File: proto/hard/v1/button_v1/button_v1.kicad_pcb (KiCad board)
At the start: 2 copper layers, 108.9 x 76.9 mm, 135 parts, among them J1 Conn_01x06_Female, J10 Conn_01x04_Male, J14 K3-2235D, J2 Conn_01x06_Female, J3 Conn_01x06_Female, J4 Conn_01x06_Female, J5 USB_B_Micro, J6 Conn_01x08_Female, J7 Conn_01x04_Female, J8 AudioJack3, J9 Conn_01x06_Male, Q1 TP0610T, Q2 IRLML2060, Q3 TP0610T, Q4 IRLML2060, Q5 IRLML2060, Q6 UMG8N, Q7 UMG8N, Q8 IRLML2803, Q9 TP0610T, U1 LCD_2.8_SPI, U10 NL27WZ14, U11 TC305, U12 LCD_1_8_SPI, U13 74HC595, U2 STM32F103C8Tx, U3 RT8009-33, U4 RClamp0554S, U5 RT9293, U6 LM339, U7 AP1117-33, U8 485, U9 LM358, Y1 8MHz

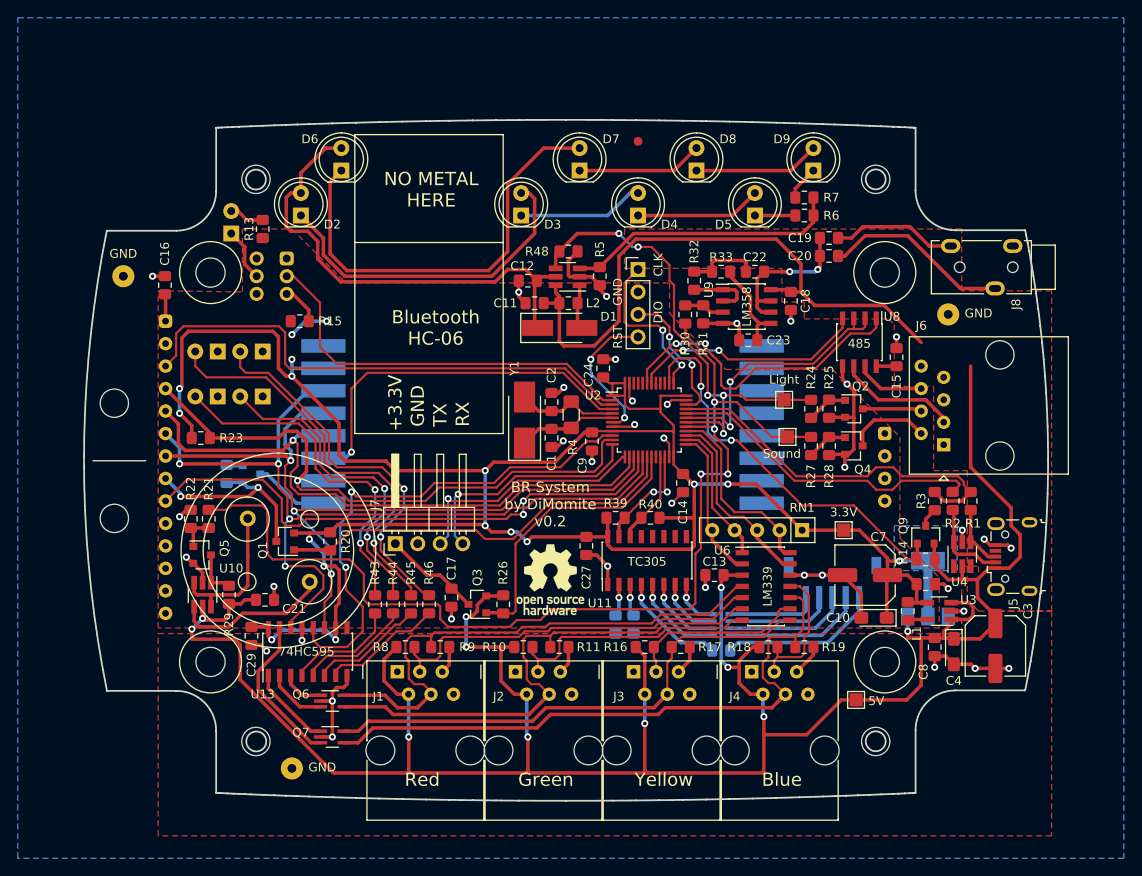
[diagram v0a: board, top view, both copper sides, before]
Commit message: Updated main board to v0.3: - changed power coils to bobbin - added test point for StartLED line - integrated new LCD screen footprint with LED power connectors - changed Schottky diode footprint to smaller in start LED converter - changed crystal footprint to smaller - added guard ring around crystal - disconnected USB shield from GND line
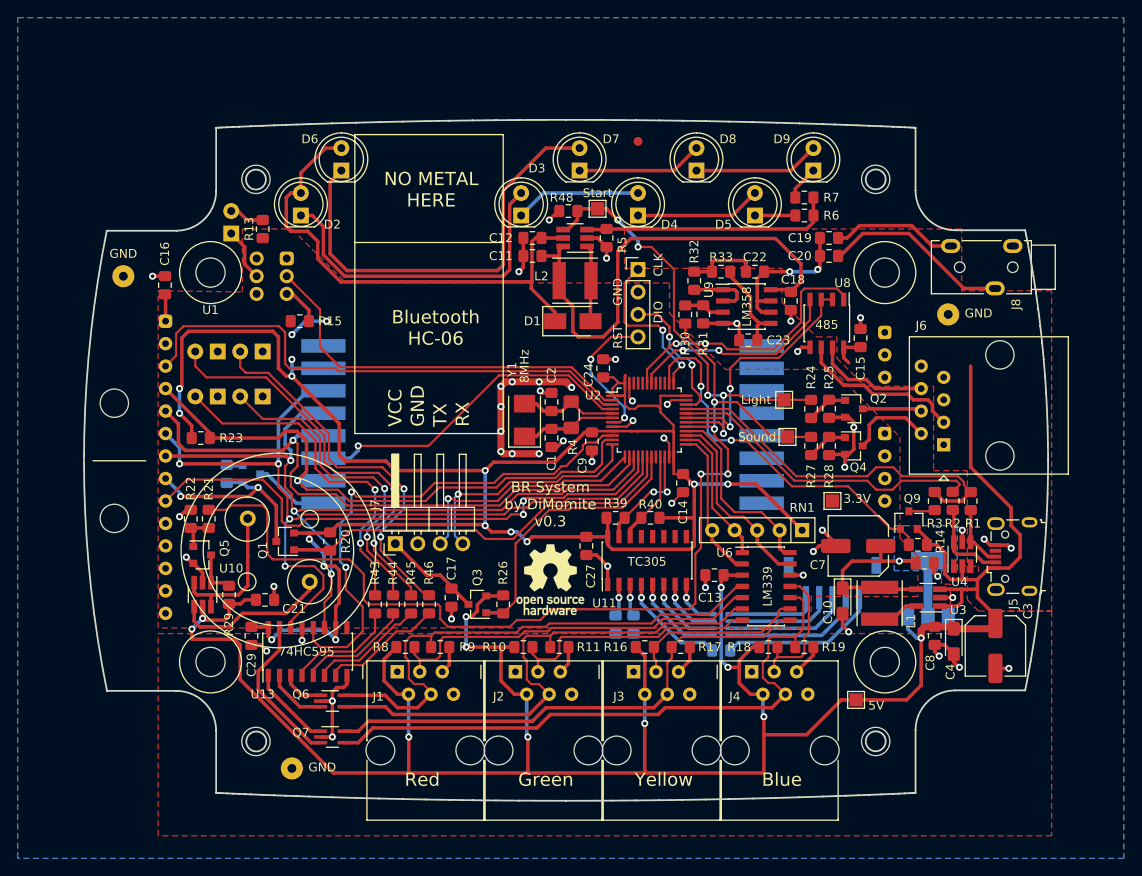
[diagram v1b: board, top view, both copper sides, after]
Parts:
- added REF**: Start, TestPoint:TestPoint_Pad_1.5x1.5mm, F.Cu at (126.5, 63.8)
- D1: footprint Diode_SMD:D_SMA_Handsoldering -> Diode_SMD:D_SMA
- L1, L2: footprint Inductor_SMD:L_0805_2012Metric_Pad1.15x1.40mm_HandSolder -> Inductor_SMD:L_Taiyo-Yuden_NR-50xx
- U1: footprint MyModules:LCD_2.8_SPI -> brbuttonsystem:LCD_2.8_SPI
- Y1: footprint Crystal:Crystal_SMD_5032-2Pin_5.0x3.2mm_HandSoldering -> Crystal:Crystal_SMD_5032-2Pin_5.0x3.2mm
- moved C11 5.34 mm to (119.1, 69.1)
- moved C12 4.85 mm to (119.1, 67.1)
- moved C15 4.61 mm to (156.2, 78.4)
- moved R48 4.57 mm to (123.2, 64.0), turned to 0 degrees
- moved U5 4.46 mm to (124.0, 67.1)
- moved R5 4.38 mm to (127.5, 67.1)
- moved U8 4.25 mm to (152.4, 76.7)
- moved C10 4.03 mm to (154.2, 108.1), turned to 270 degrees
- moved REF** 3.54 mm to (153.0, 96.8)
- moved C7 3.39 mm to (156.0, 101.9)
- moved L1 3.30 mm to (158.4, 108.3)
- moved L2 2.65 mm to (124.0, 71.9)
- moved Q9 2.52 mm to (161.7, 98.9)
- moved C6 2.42 mm to (163.4, 103.8)
- moved U3 1.98 mm to (163.8, 107.7)
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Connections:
- J5 pad 6: GND -> Net-(J5-Pad6)
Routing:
- net +5V: track 343.1 -> 333.3 mm
- net GND: track 129.9 -> 137.0 mm, vias 37 -> 50
- net /EXT_READ: track 36.4 -> 30.9 mm
- net /Entertainment/EXT_B: track 7.85 -> 13.1 mm
- net /Entertainment/EXT_A: track 13.7 -> 18.8 mm
- net /Entertainment/StartLedOut: track 54.2 -> 58.4 mm
- net /BACK_LCD_CS: track 42.6 -> 38.4 mm
- net +3V3: track 264.6 -> 260.6 mm
- net Net-(D1-Pad2): track 5.13 -> 8.66 mm
- net /USB_PULLUP: track 45.6 -> 42.7 mm
- net Net-(R5-Pad2): track 31.4 -> 28.7 mm
- net /EXT_RW: track 30.5 -> 27.8 mm
- net /EXT_WRITE: track 26.7 -> 24.1 mm
- net Net-(L1-Pad1): track 2.24 -> 4.73 mm
- net Net-(Q9-Pad3): track 2.20 -> 2.97 mm
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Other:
- board text added: "BR System by DiMomite v0.3"
- board text added: "VCC"
- board text removed: "+3.3V"
- board text removed: "BR System by DiMomite v0.2"

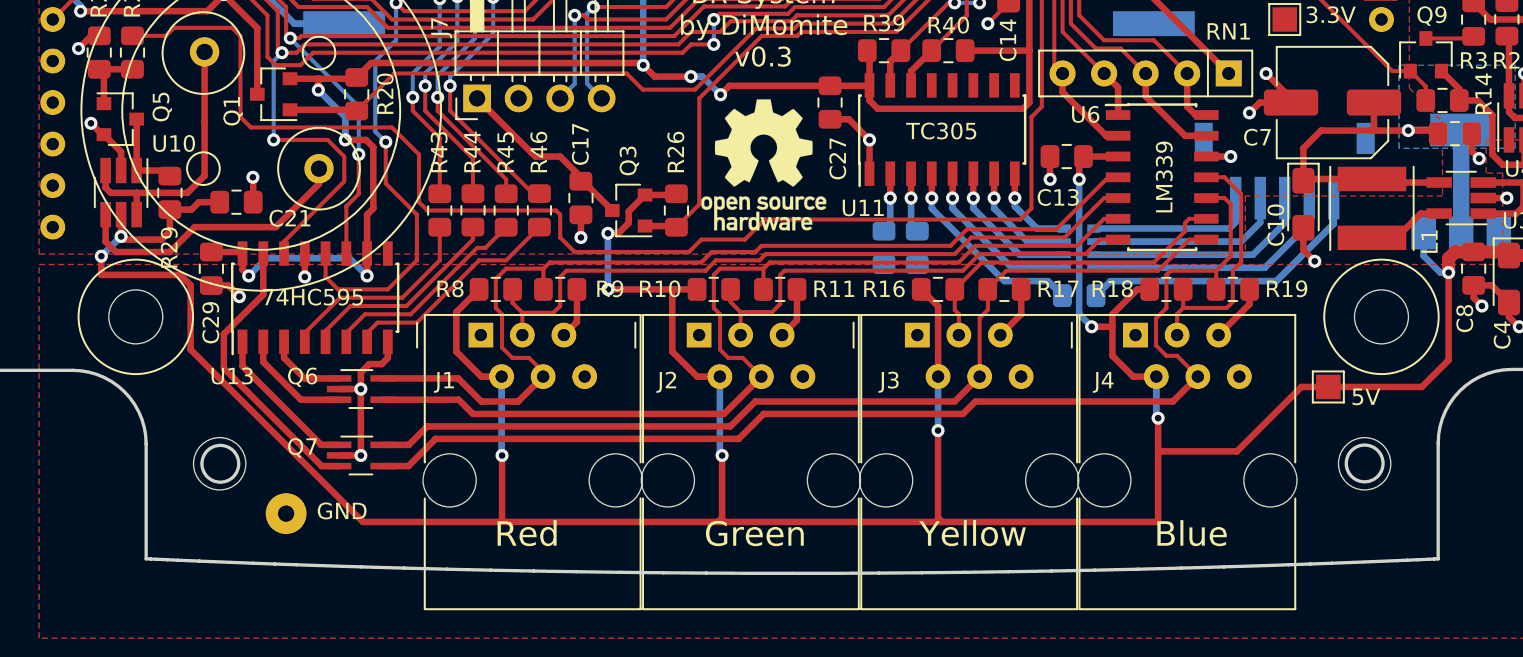
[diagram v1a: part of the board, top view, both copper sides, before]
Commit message: Moved buttons to separate sheet. Added replacement transistors for buttons.
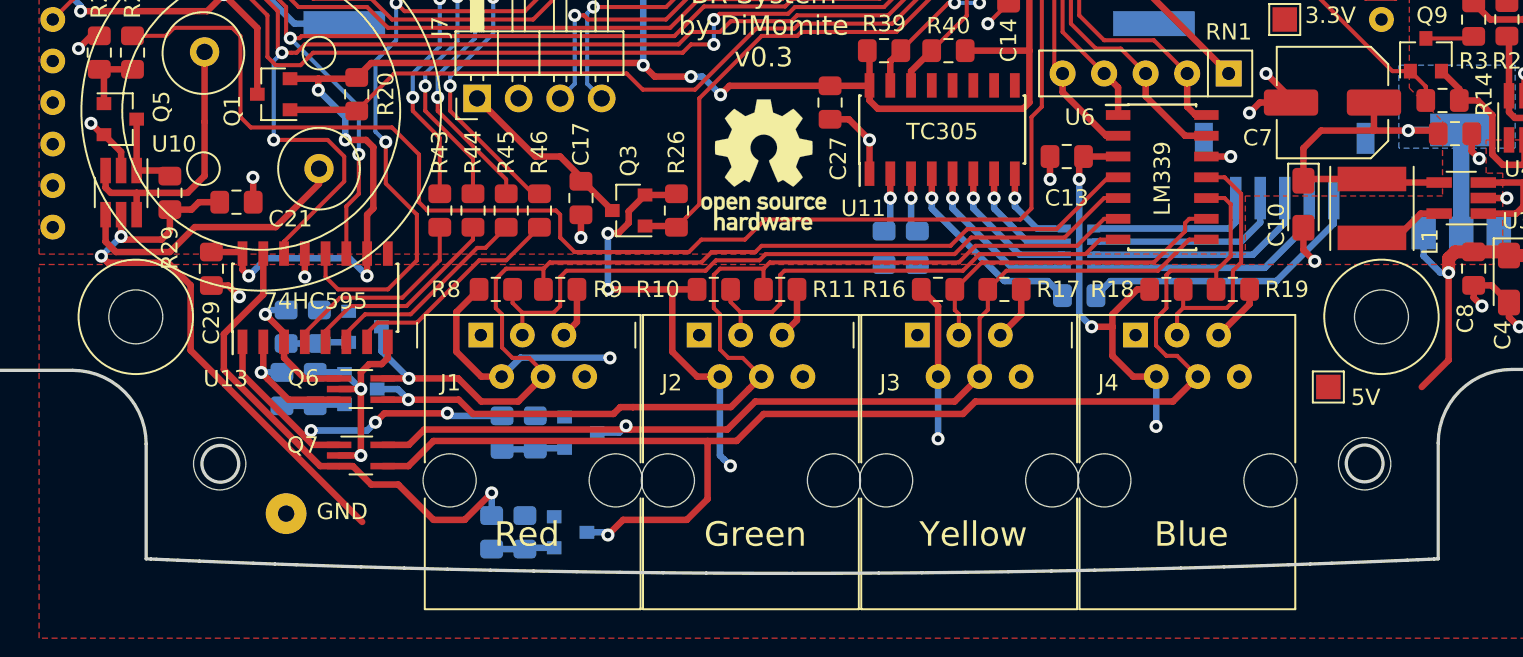
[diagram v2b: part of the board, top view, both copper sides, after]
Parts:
- added Q10: Q_NPN_BEC, Package_TO_SOT_SMD:SOT-23, B.Cu at (96.8, 115.6)
- added Q11: Q_NPN_BEC, Package_TO_SOT_SMD:SOT-23, B.Cu at (109.3, 128.1)
- added Q12: Q_NPN_BEC, Package_TO_SOT_SMD:SOT-23, B.Cu at (96.5, 119.4)
- added Q13: Q_NPN_BEC, Package_TO_SOT_SMD:SOT-23, B.Cu at (110.0, 122.0)
- added R35: 1k, Resistor_SMD:R_0805_2012Metric_Pad1.15x1.40mm_HandSolder, B.Cu at (91.9, 115.6)
- added R36: 1k, Resistor_SMD:R_0805_2012Metric_Pad1.15x1.40mm_HandSolder, B.Cu at (104.5, 128.1)
- added R37: 1k, Resistor_SMD:R_0805_2012Metric_Pad1.15x1.40mm_HandSolder, B.Cu at (94.0, 115.6)
- added R38: 1k, Resistor_SMD:R_0805_2012Metric_Pad1.15x1.40mm_HandSolder, B.Cu at (106.6, 128.1)
- added R41: 1k, Resistor_SMD:R_0805_2012Metric_Pad1.15x1.40mm_HandSolder, B.Cu at (91.7, 119.4)
- added R42: 1k, Resistor_SMD:R_0805_2012Metric_Pad1.15x1.40mm_HandSolder, B.Cu at (105.2, 122.0)
- added R47: 1k, Resistor_SMD:R_0805_2012Metric_Pad1.15x1.40mm_HandSolder, B.Cu at (93.7, 119.4)
- added R49: 1k, Resistor_SMD:R_0805_2012Metric_Pad1.15x1.40mm_HandSolder, B.Cu at (107.2, 122.0)
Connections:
- net /PLAY_LED0 renamed /Buttons/PLAY_LED0
- net /PLAY_LED1 renamed /Buttons/PLAY_LED1
- net /PLAY_LED2 renamed /Buttons/PLAY_LED2
- net /PLAY_LED3 renamed /Buttons/PLAY_LED3
- net Net-(J1-Pad4) renamed /Buttons/BPRESS_0
- net Net-(J2-Pad4) renamed /Buttons/BPRESS_1
- net Net-(J3-Pad4) renamed /Buttons/BPRESS_3
- net Net-(J4-Pad4) renamed /Buttons/BPRESS_2
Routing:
- net +5V: track 333.3 -> 250.1 mm
- net /Buttons/PLAY_LED1: track 9.62 -> 22.7 mm, vias 0 -> 3
- net /Buttons/PLAY_LED0: track 17.3 -> 30.1 mm, vias 0 -> 1
- net /Buttons/BPRESS_2: track 70.5 -> 82.4 mm, vias 0 -> 1
- net Net-(Q10-Pad1): track 0.00 -> 3.86 mm
- net Net-(Q11-Pad1): track 0.00 -> 3.86 mm
- net Net-(Q12-Pad1): track 0.00 -> 3.86 mm
- net Net-(Q13-Pad1): track 0.00 -> 3.86 mm
- net /Buttons/BPRESS_0: track 60.7 -> 64.6 mm, vias 0 -> 1
- net /Buttons/PLAY_LED3: track 5.10 -> 8.63 mm, vias 0 -> 1
- net GND: track 137.0 -> 140.2 mm
- net /Buttons/BPRESS_3: track 58.4 -> 60.7 mm, vias 0 -> 1
- net /Buttons/BPRESS_1: track 59.8 -> 62.0 mm, vias 0 -> 1
- net /Buttons/PLAY_LED2: track 7.05 -> 8.88 mm, vias 0 -> 1
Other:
- board text added: "!!! Offset buttons connectors by 4 mm from center right !!!"
- board text added: "For Q6"
- board text added: "For Q7"
- board text removed: "!!! Offset by 4 mm from center !!!"

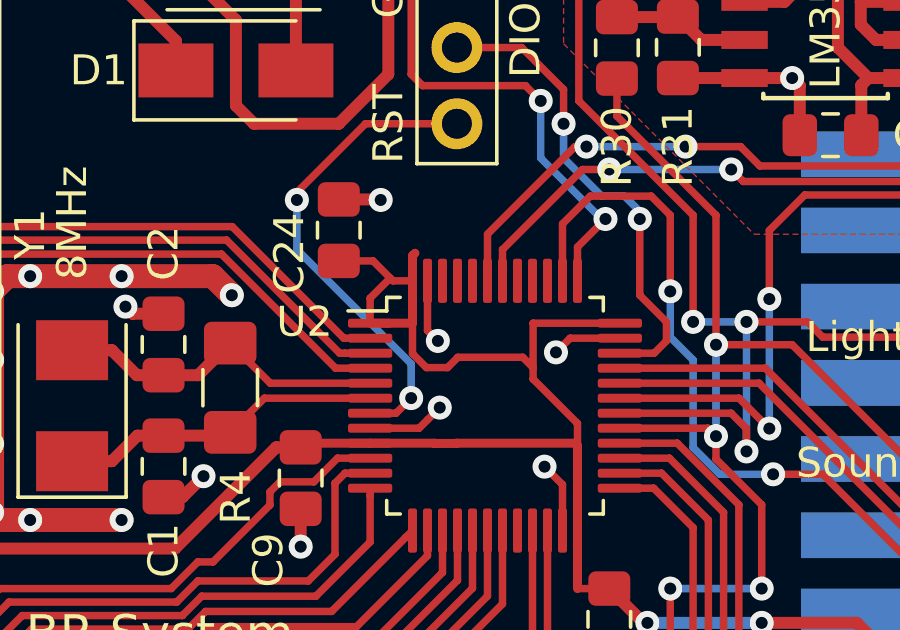
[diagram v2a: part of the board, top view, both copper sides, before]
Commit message: BOOT0 connected to GND Due to migration to Kicad V5.1.6 had to change text style from "bold" to "normal"
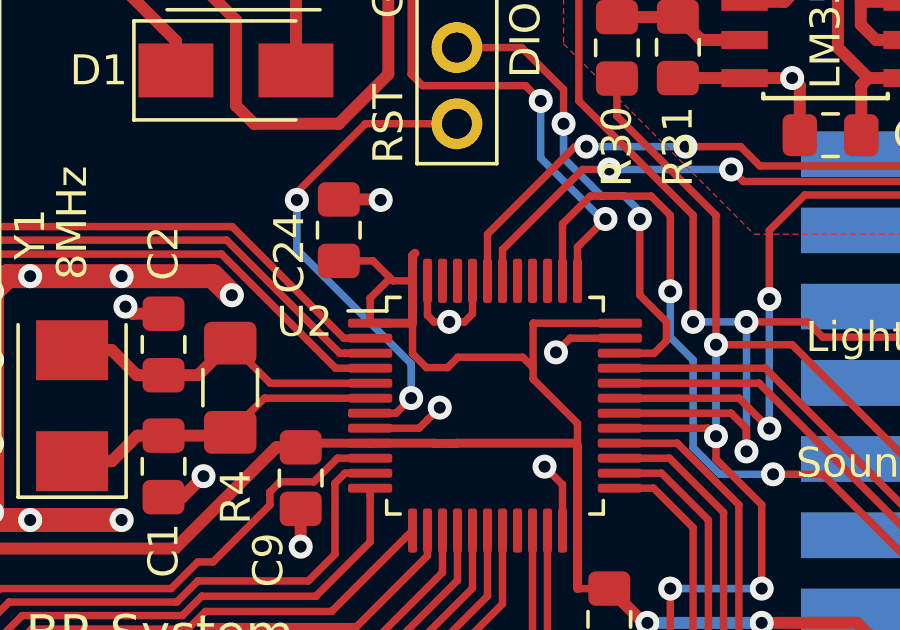
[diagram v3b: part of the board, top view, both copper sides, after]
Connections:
- U2 pad 44: /BOOT0 -> GND
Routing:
- net GND: track 140.2 -> 142.1 mm

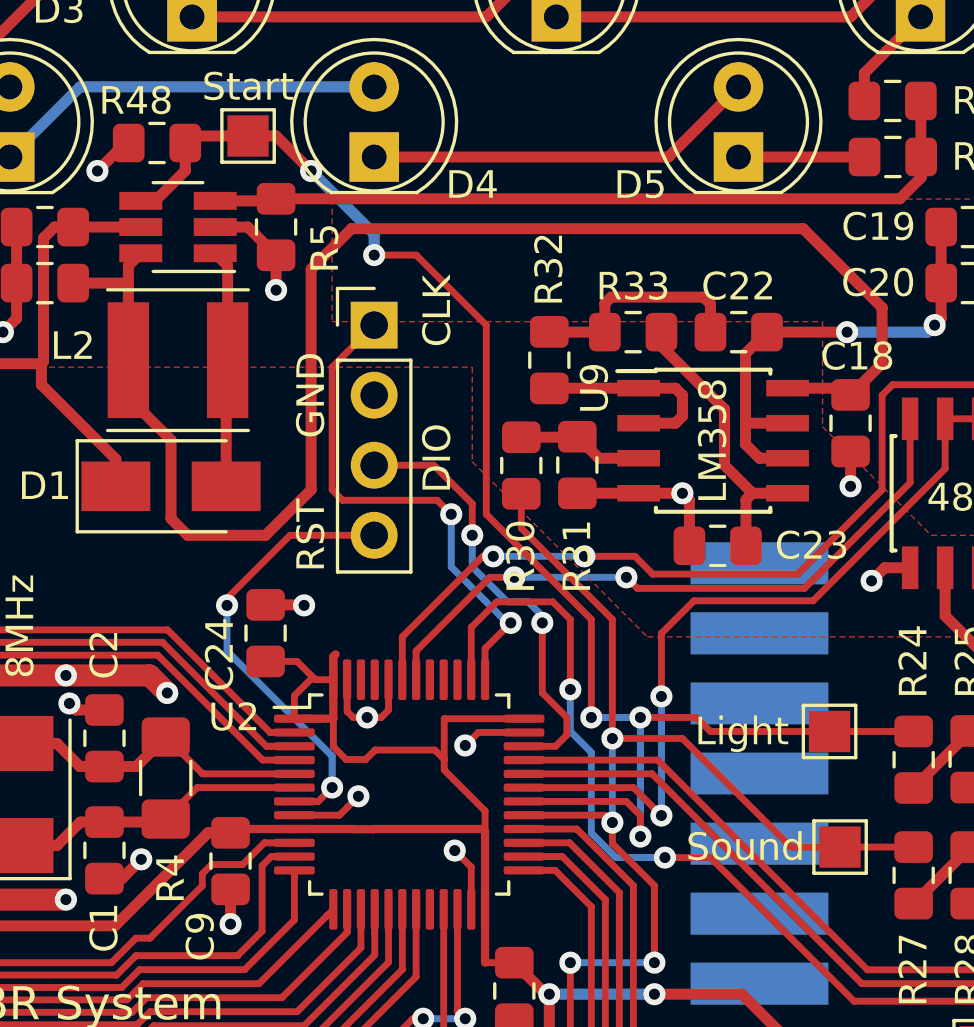
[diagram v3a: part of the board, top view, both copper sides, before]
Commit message: Debug connector updates: - added +3.3 connection - pins reorganized to match ST Link layout
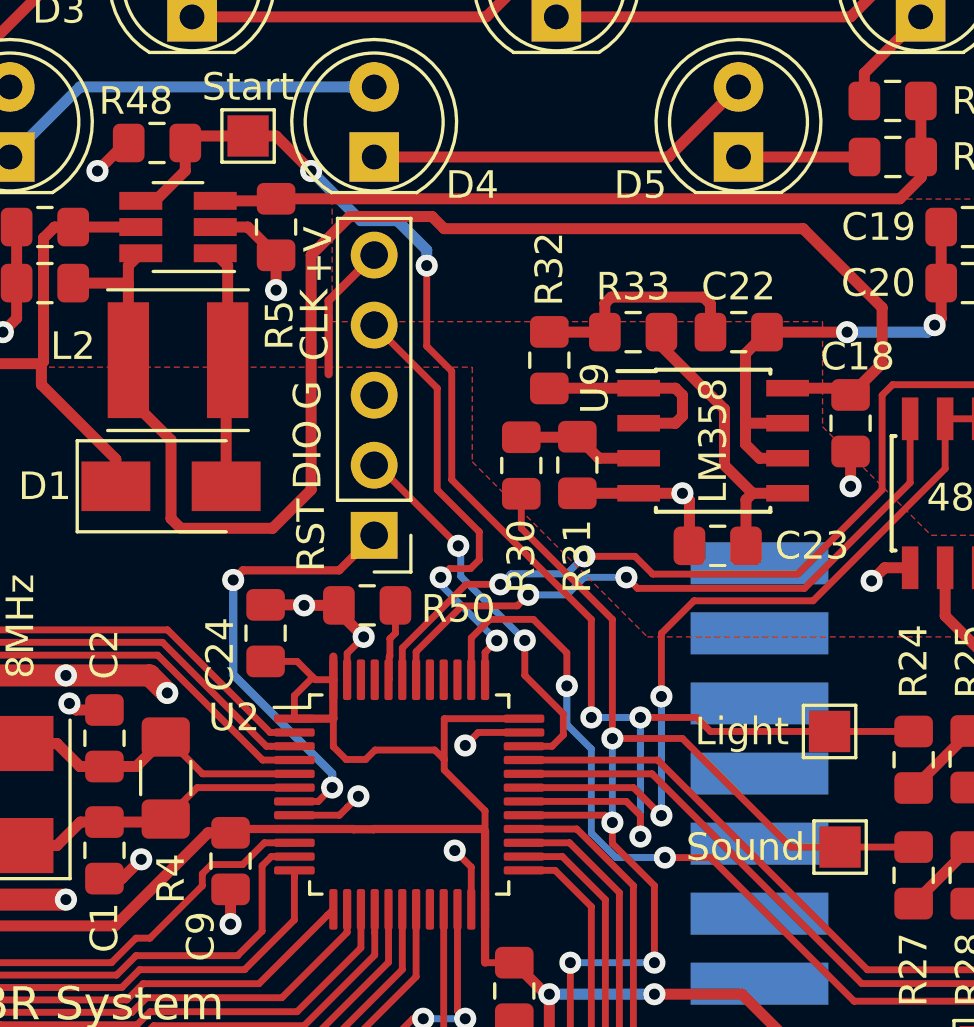
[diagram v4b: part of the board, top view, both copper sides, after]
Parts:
- added R50: 100k, Resistor_SMD:R_0805_2012Metric_Pad1.15x1.40mm_HandSolder, F.Cu at (130.8, 80.8)
- J10: value Conn_01x04_Male -> Conn_01x05_Male; footprint Connector_PinHeader_2.54mm:PinHeader_1x04_P2.54mm_Vertical -> Connector_PinHeader_2.54mm:PinHeader_1x05_P2.54mm_Vertical
- moved J10 7.62 mm to (131.1, 78.2), turned to 180 degrees
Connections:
- J10 pad 1: /SWCLK -> /NRST
- J10 pad 2: GND -> /SWDIO
- J10 pad 3: /SWDIO -> GND
- J10 pad 4: /NRST -> /SWCLK
- U2 pad 44: GND -> /BOOT0
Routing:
- net +3V3: track 260.6 -> 265.5 mm
- net /BOOT0: track 0.00 -> 2.80 mm
- net /SWCLK: track 18.6 -> 16.5 mm
- net /SWDIO: track 16.1 -> 14.3 mm
- net /USB_PULLUP: track 42.7 -> 41.1 mm
- net GND: track 142.1 -> 142.7 mm
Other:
- board text added: "+V"
- board text added: "G"
